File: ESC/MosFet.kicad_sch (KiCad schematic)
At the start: 30 parts, among them J2 load, J3 load, J4 load, Q1 BSC028N06LS3, Q2 BSC028N06LS3, U2 IRS2101

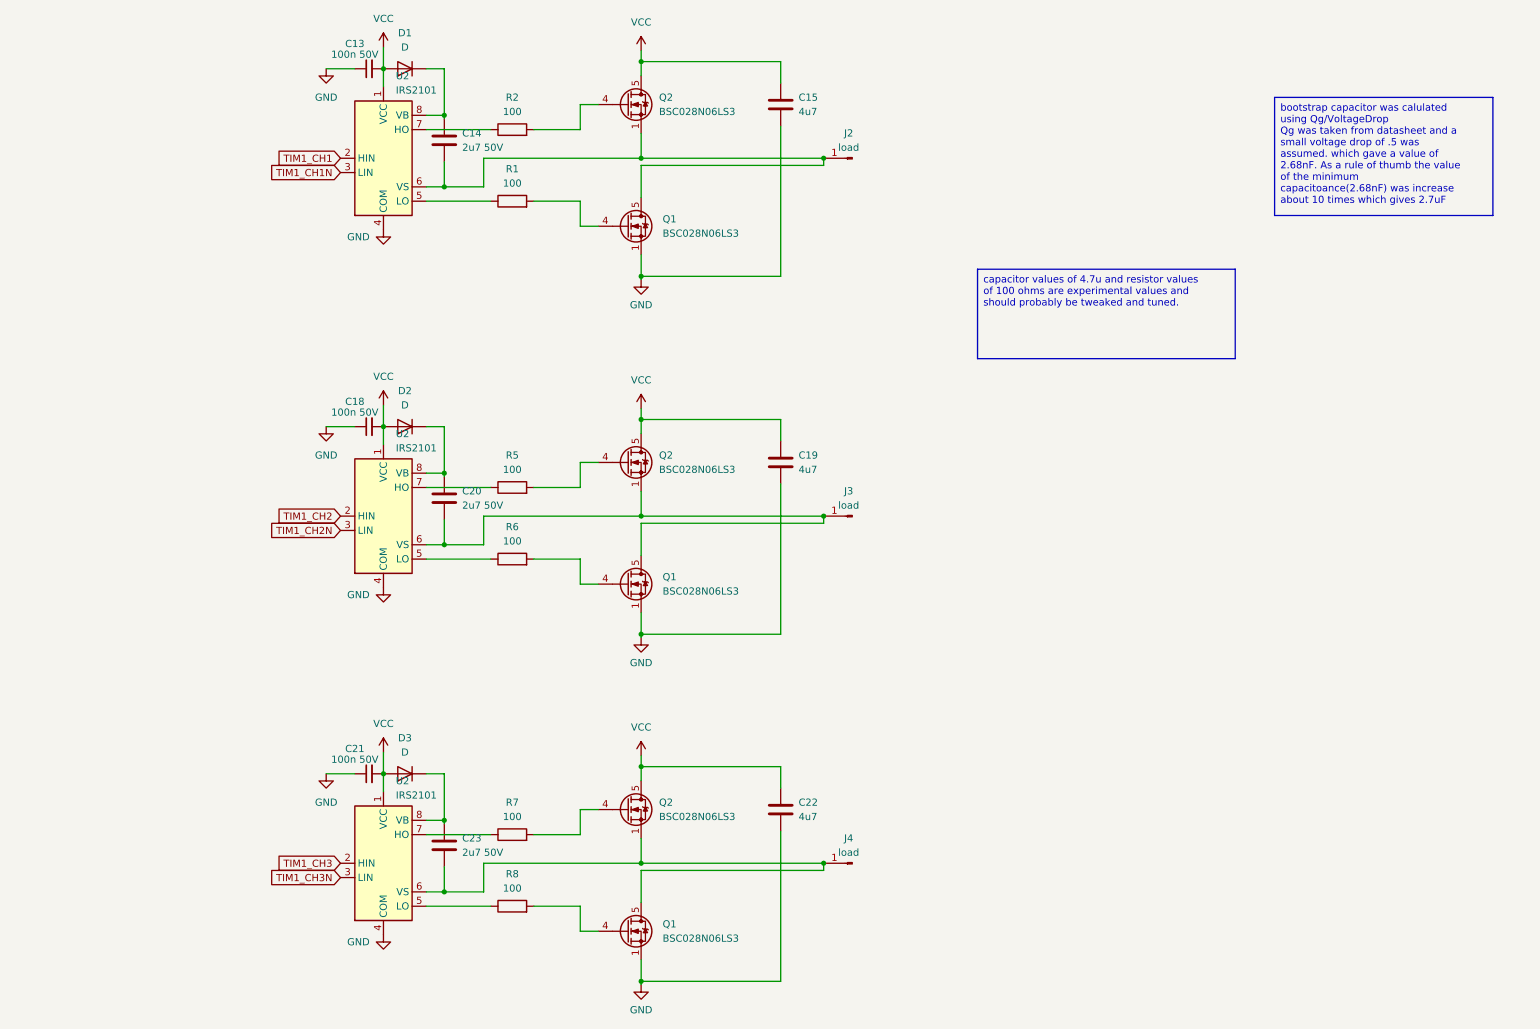
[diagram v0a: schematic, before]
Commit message: finished first mock up of the esc scheamtic still need to check everything works tho
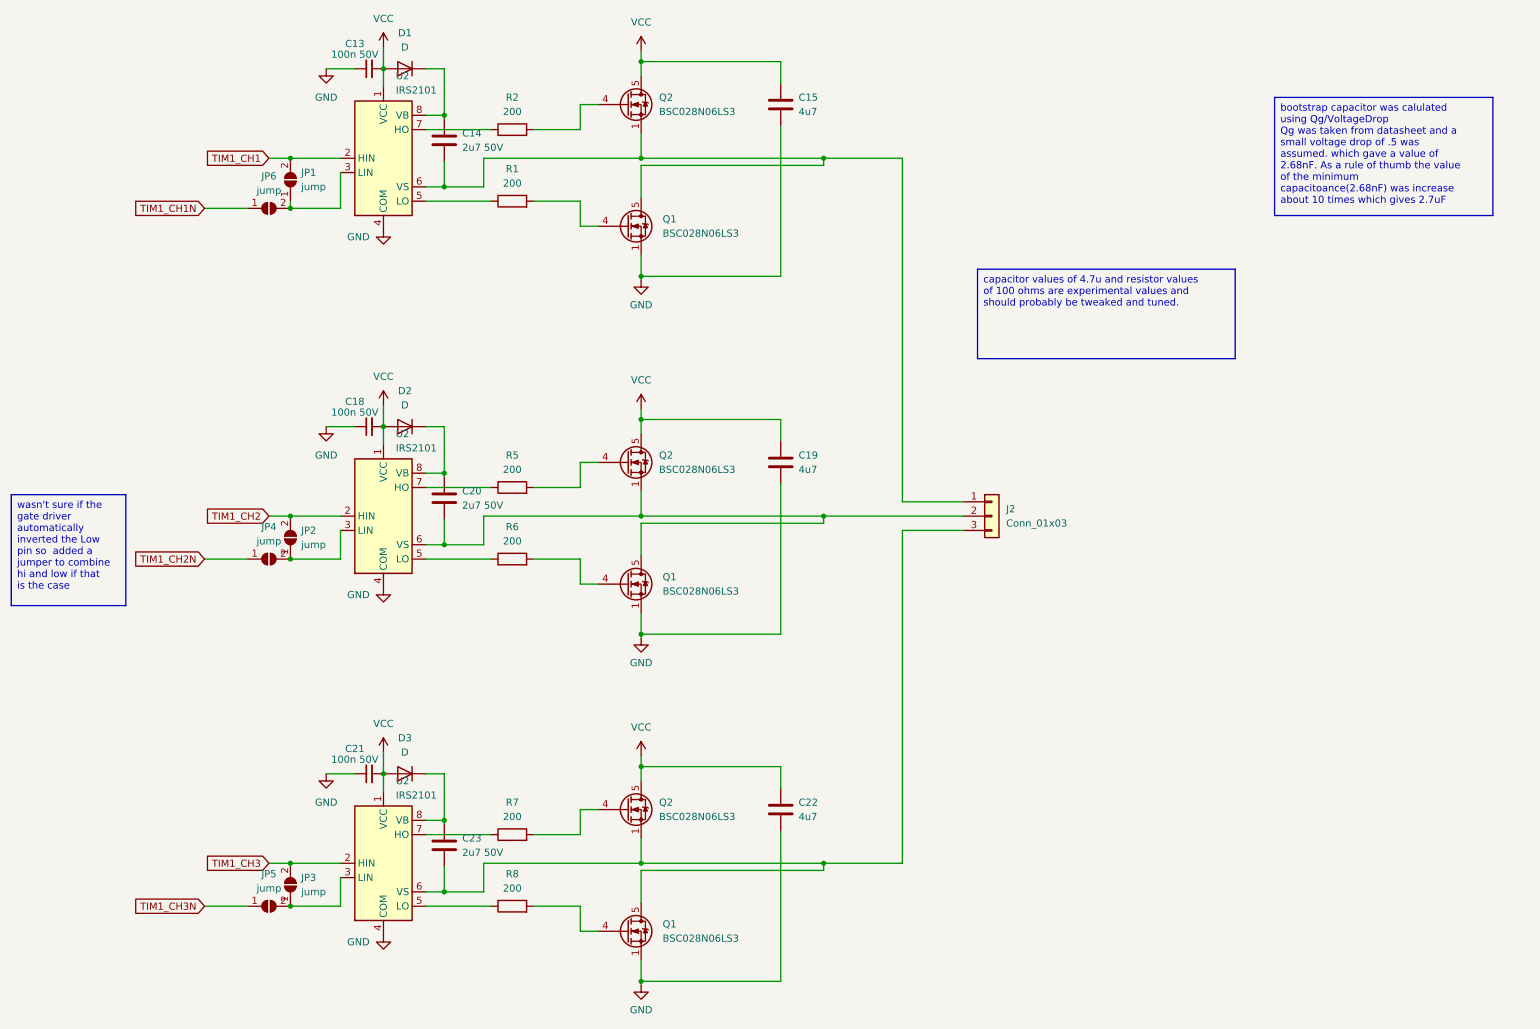
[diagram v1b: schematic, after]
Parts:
- removed J2, J3, J4: load, symbol Connector:Conn_01x01_Pin
- added J2: Conn_01x03, TerminalBlock_Phoenix:TerminalBlock_Phoenix_MKDS-1,5-3_1x03_P5.00mm_Horizontal, symbol Connector_Generic:Conn_01x03
- added JP1, JP2, JP3, JP4, JP5, JP6: jump, Capacitor_SMD:C_0603_1608Metric_Pad1.08x0.95mm_HandSolder, symbol Jumper:SolderJumper_2_Open
- C13, C14, C15, C18, C19, C20, C21, C22, C23: footprint (none) -> Capacitor_SMD:C_0603_1608Metric_Pad1.08x0.95mm_HandSolder
- D1, D2, D3: footprint (none) -> Diode_SMD:D_0603_1608Metric_Pad1.05x0.95mm_HandSolder
- R1, R2, R5, R6, R7, R8: value 100 -> 200; footprint (none) -> Resistor_SMD:R_2512_6332Metric_Pad1.40x3.35mm_HandSolder
- U2: footprint (none) -> Package_SO:SOIC-8-1EP_3.9x4.9mm_P1.27mm_EP2.41x3.81mm
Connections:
- net TIM1_CH1: now also JP1.2 (B)
- net TIM1_CH1N: now also JP6.1 (A); no longer U2.3 (LIN)
- net TIM1_CH2: now also JP2.2 (B)
- net TIM1_CH2N: now also JP4.1 (A); no longer U2.3 (LIN)
- net TIM1_CH3: now also JP3.2 (B)
- net TIM1_CH3N: now also JP5.1 (A); no longer U2.3 (LIN)
- net at C14.2, Q1.5 (D), Q2.1 (S)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: now also J2.1 (Pin_1)
- net at C20.2, Q1.5 (D), Q2.1 (S)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: now also J2.2 (Pin_2)
- net at C23.2, Q1.5 (D), Q2.1 (S)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: now also J2.3 (Pin_3)
- new net: JP1.1 (A), JP6.2 (B), U2.3 (LIN)
- new net: JP3.1 (A), JP5.2 (B), U2.3 (LIN)
- new net: JP2.1 (A), JP4.2 (B), U2.3 (LIN)

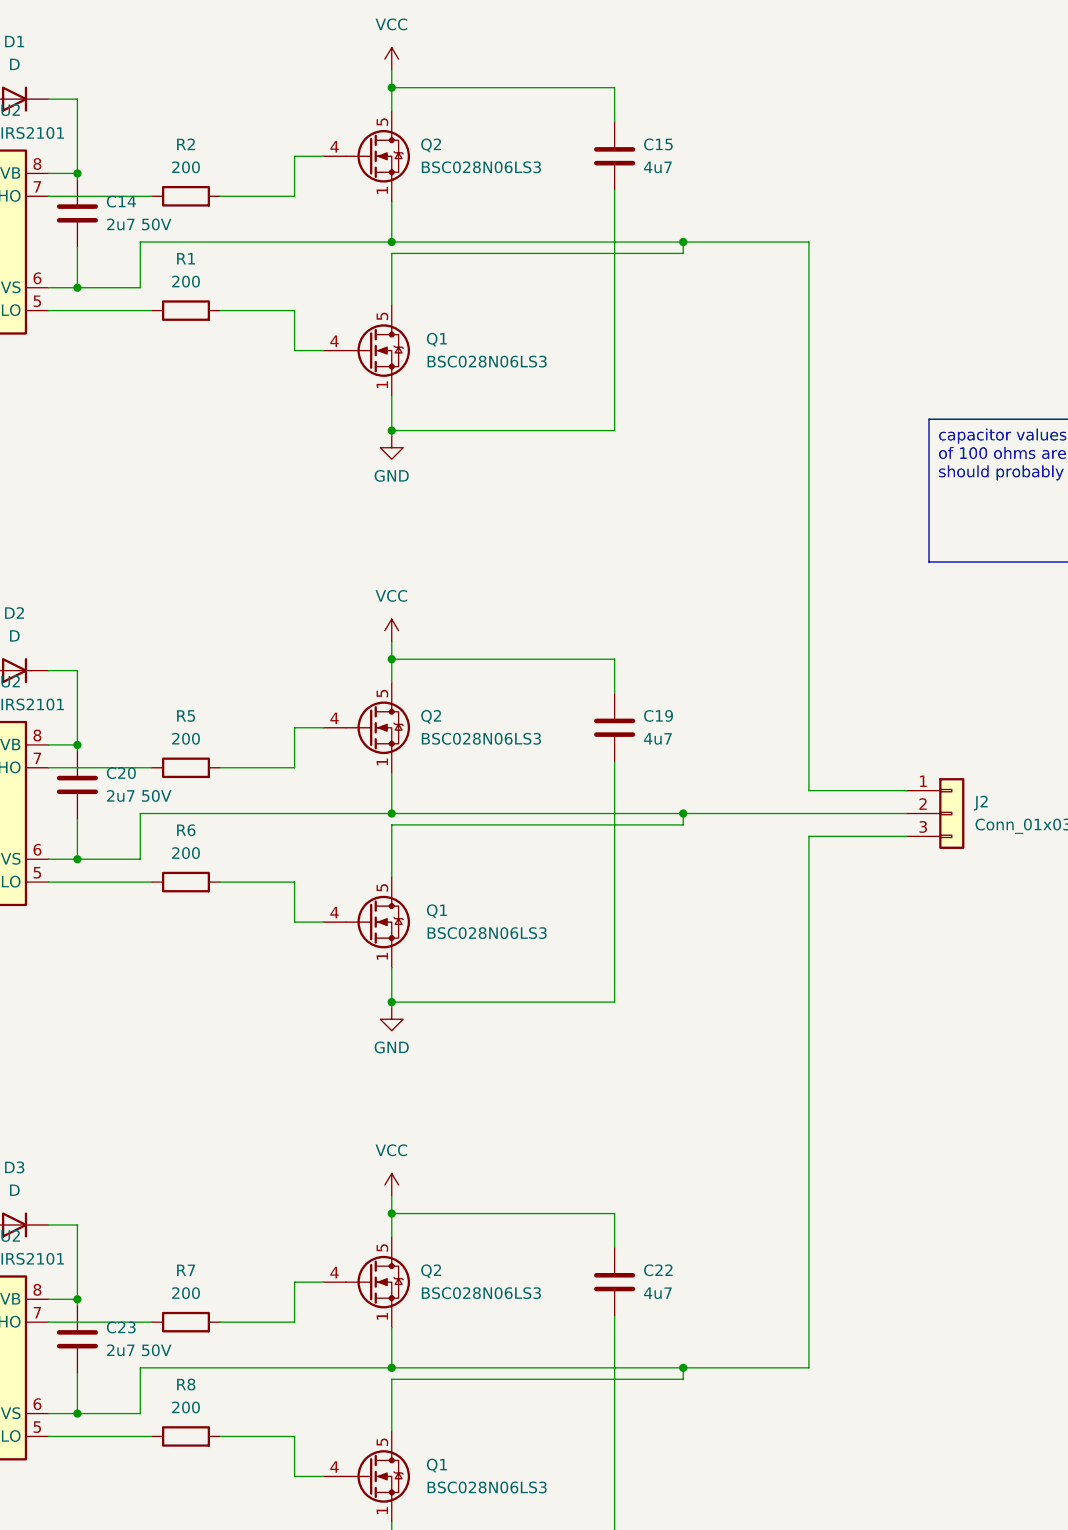
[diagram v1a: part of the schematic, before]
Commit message: finished a mockup of the pcb layout
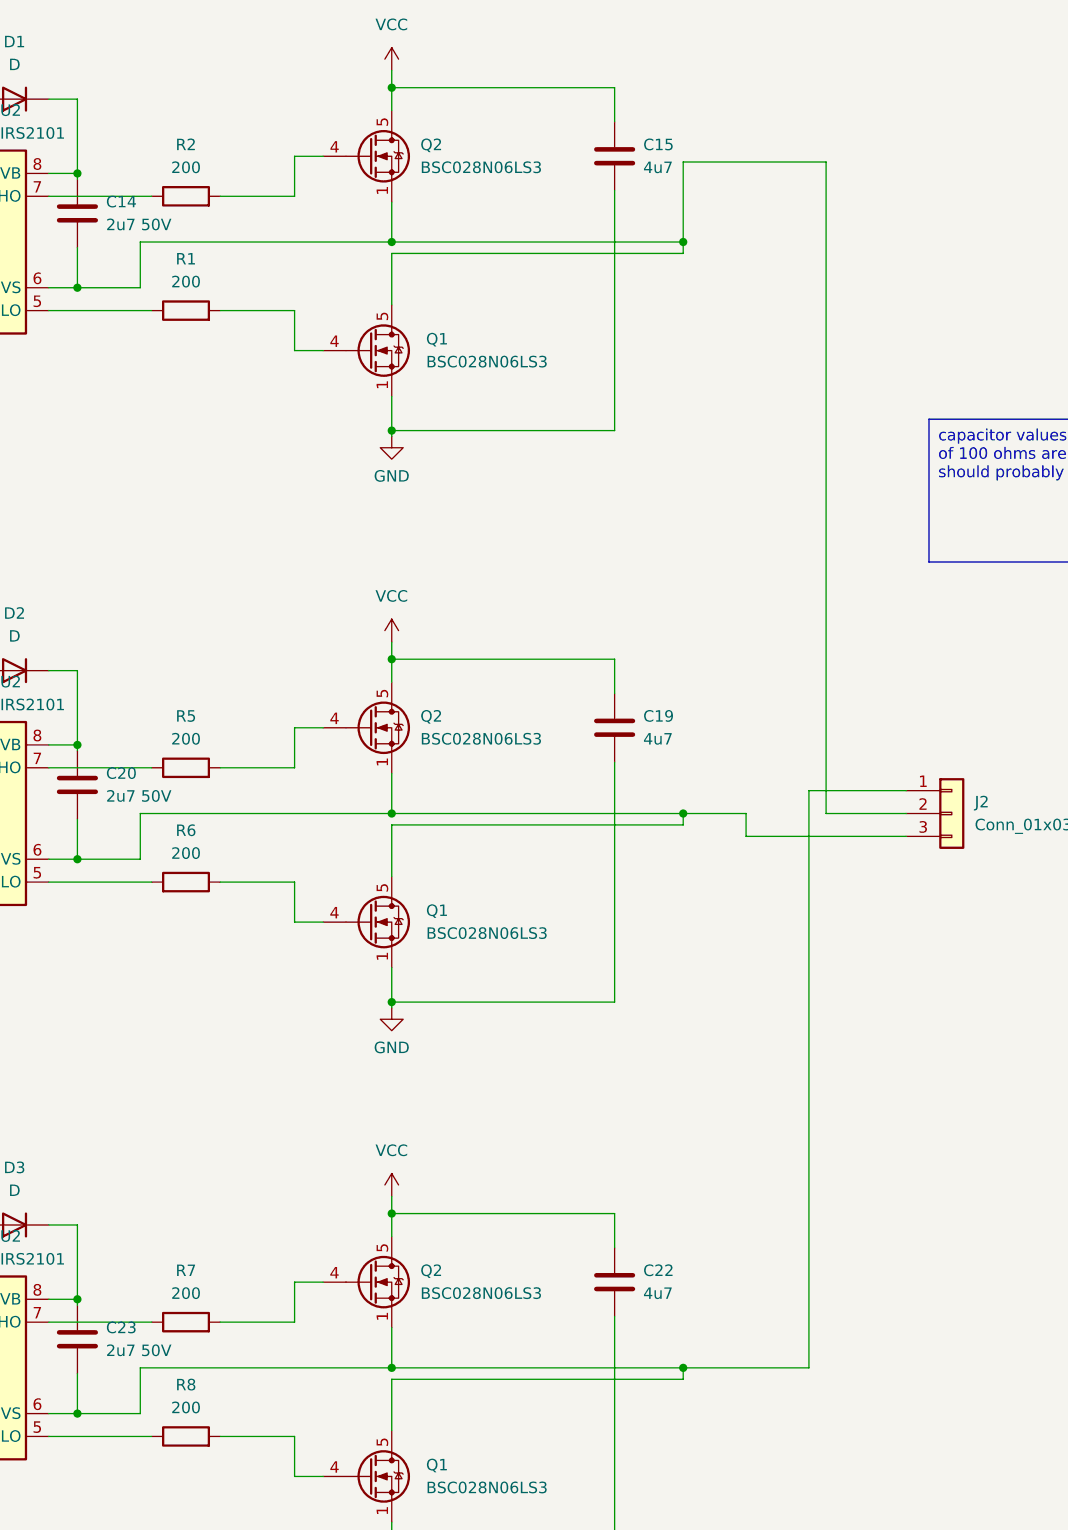
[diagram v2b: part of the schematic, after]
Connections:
- net at C14.2, Q1.5 (D), Q2.1 (S)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: now also J2.2 (Pin_2); no longer J2.1 (Pin_1)
- net at Q1.4 (G): now also R6.1; no longer R6.2
- net at C20.2, Q1.5 (D), Q2.1 (S)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: now also J2.3 (Pin_3); no longer J2.2 (Pin_2)
- net at U2.5 (LO): now also R6.2; no longer R6.1
- net at C23.2, Q1.5 (D), Q2.1 (S)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: now also J2.1 (Pin_1); no longer J2.3 (Pin_3)
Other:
- moved on the sheet: R6
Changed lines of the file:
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@@
   (junction (at 124.46 31.75) (diameter 0) (color 0 0 0 0)
   )
+  (junction (at 156.845 112.395) (diameter 0) (color 0 0 0 0)
+  )
   (junction (at 124.46 112.395) (diameter 0) (color 0 0 0 0)
   )
@@
   (junction (at 156.845 48.895) (diameter 0) (color 0 0 0 0)
   )
-  (junction (at 156.845 112.395) (diameter 0) (color 0 0 0 0)
-  )
   (junction (at 89.535 166.37) (diameter 0) (color 0 0 0 0)
   )
@@
     (stroke (width 0) (type default))
   )
-  (wire (pts (xy 156.845 48.895) (xy 170.815 48.895))
+  (wire (pts (xy 156.845 40.005) (xy 172.72 40.005))
     (stroke (width 0) (type default))
   )
@@
     (stroke (width 0) (type default))
   )
-  (wire (pts (xy 170.815 109.855) (xy 181.61 109.855))
-    (stroke (width 0) (type default))
-  )
   (wire (pts (xy 89.535 179.07) (xy 96.52 179.07))
     (stroke (width 0) (type default))
@@
     (stroke (width 0) (type default))
   )
+  (wire (pts (xy 170.815 109.855) (xy 181.61 109.855))
+    (stroke (width 0) (type default))
+  )
   (wire (pts (xy 149.225 106.68) (xy 149.225 133.35))
     (stroke (width 0) (type default))
@@
     (stroke (width 0) (type default))
   )
-  (wire (pts (xy 170.815 173.99) (xy 170.815 114.935))
+  (wire (pts (xy 170.815 109.855) (xy 170.815 173.99))
     (stroke (width 0) (type default))
   )
@@
     (stroke (width 0) (type default))
   )
+  (wire (pts (xy 156.845 112.395) (xy 163.83 112.395))
+    (stroke (width 0) (type default))
+  )
+  (wire (pts (xy 172.72 40.005) (xy 172.72 112.395))
+    (stroke (width 0) (type default))
+  )
   (wire (pts (xy 78.74 29.21) (xy 78.74 33.02))
     (stroke (width 0) (type default))
@@
     (stroke (width 0) (type default))
   )
+  (wire (pts (xy 172.72 112.395) (xy 181.61 112.395))
+    (stroke (width 0) (type default))
+  )
   (wire (pts (xy 156.845 113.665) (xy 156.845 112.395))
     (stroke (width 0) (type default))
@@
     (stroke (width 0) (type default))
   )
-  (wire (pts (xy 170.815 48.895) (xy 170.815 109.855))
-    (stroke (width 0) (type default))
-  )
   (wire (pts (xy 113.665 39.37) (xy 116.84 39.37))
     (stroke (width 0) (type default))
@@
     (stroke (width 0) (type default))
   )
-  (wire (pts (xy 170.815 114.935) (xy 181.61 114.935))
-    (stroke (width 0) (type default))
-  )
   (wire (pts (xy 62.23 48.895) (xy 71.12 48.895))
     (stroke (width 0) (type default))
@@
     (stroke (width 0) (type default))
   )
+  (wire (pts (xy 163.83 114.935) (xy 181.61 114.935))
+    (stroke (width 0) (type default))
+  )
   (wire (pts (xy 86.36 166.37) (xy 89.535 166.37))
     (stroke (width 0) (type default))
@@
     (stroke (width 0) (type default))
   )
-  (wire (pts (xy 156.845 112.395) (xy 181.61 112.395))
-    (stroke (width 0) (type default))
-  )
   (wire (pts (xy 86.36 168.91) (xy 97.79 168.91))
     (stroke (width 0) (type default))
@@
     (stroke (width 0) (type default))
   )
+  (wire (pts (xy 163.83 112.395) (xy 163.83 114.935))
+    (stroke (width 0) (type default))
+  )
   (wire (pts (xy 89.535 166.37) (xy 89.535 158.115))
     (stroke (width 0) (type default))
   )
+  (wire (pts (xy 156.845 40.005) (xy 156.845 48.895))
+    (stroke (width 0) (type default))
+  )
   (wire (pts (xy 62.23 120.015) (xy 71.12 120.015))
     (stroke (width 0) (type default))
@@
     )
   )
-  (symbol (lib_id "Device:R") (at 101.6 120.015 90) (unit 1)
-    (in_bom yes) (on_board yes) (dnp no) (fields_autoplaced)
+  (symbol (lib_id "Device:R") (at 101.6 120.015 270) (mirror x) (unit 1)
+    (in_bom yes) (on_board yes) (dnp no)
     (property "Reference" "R6" (at 101.6 114.3 90)
       (effects (font (size 1.27 1.27)))
@@
   )
   (symbol (lib_id "Device:C") (at 89.535 170.815 0) (unit 1)
-    (in_bom yes) (on_board yes) (dnp no) (fields_autoplaced)
+    (in_bom yes) (on_board yes) (dnp no)
     (property "Reference" "C23" (at 92.71 169.545 0)
       (effects (font (size 1.27 1.27)) (justify left))
